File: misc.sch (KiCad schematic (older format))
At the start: 11 parts, among them J11 USB_OTG, U3 LP5900SDX-2.8, U4 AP2204R-3.0TRG1

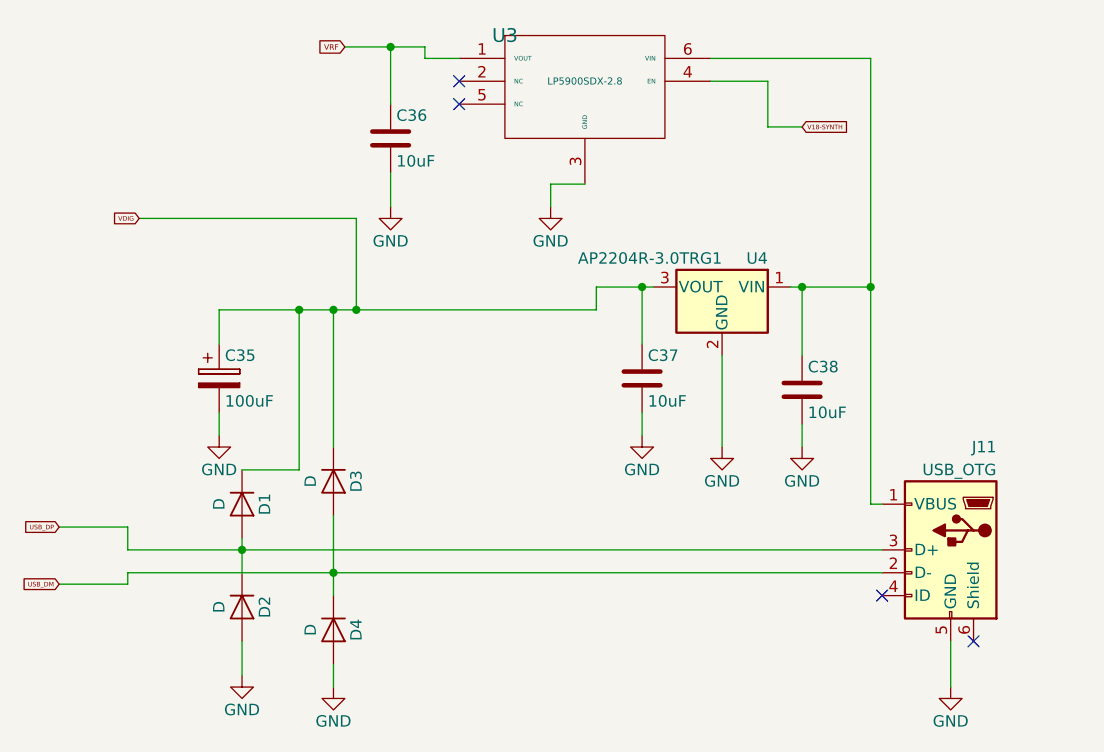
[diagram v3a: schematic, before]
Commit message: use external oscillator repace xtal and add a led
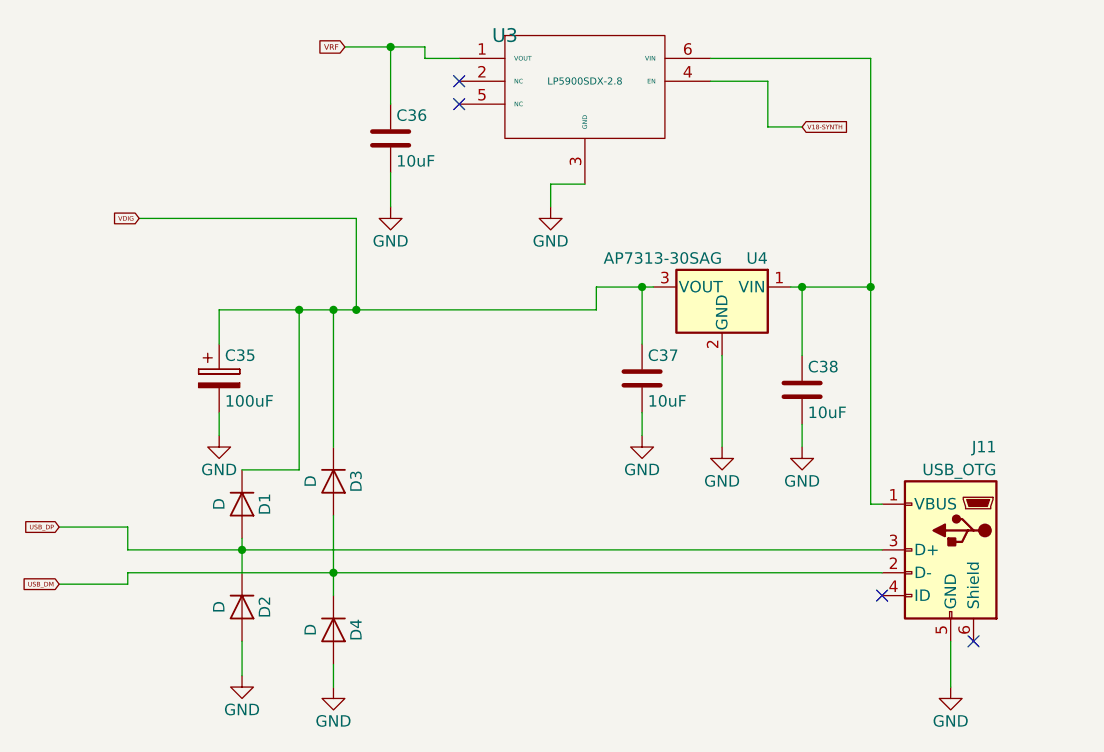
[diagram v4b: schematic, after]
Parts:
- U4: value AP2204R-3.0TRG1 -> AP7313-30SAG
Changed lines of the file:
@@
 Connection ~ 5100 3800
 $Comp
-L GND #PWR36
+L GND #PWR38
 U 1 1 5C690F71
 P 4700 4250
-F 0 "#PWR36" H 4700 4000 50  0001 C CNN
+F 0 "#PWR38" H 4700 4000 50  0001 C CNN
 F 1 "GND" H 4700 4100 50  0000 C CNN
 F 2 "" H 4700 4250 50  0001 C CNN
@@
 $EndComp
 $Comp
-L GND #PWR37
+L GND #PWR39
 U 1 1 5C690F9B
 P 5100 4300
-F 0 "#PWR37" H 5100 4050 50  0001 C CNN
+F 0 "#PWR39" H 5100 4050 50  0001 C CNN
 F 1 "GND" H 5100 4150 50  0000 C CNN
 F 2 "" H 5100 4300 50  0001 C CNN
@@
 	4200 3850 3900 3850
 $Comp
-L GND #PWR35
+L GND #PWR37
 U 1 1 5C6911FA
 P 4600 3200
-F 0 "#PWR35" H 4600 2950 50  0001 C CNN
+F 0 "#PWR37" H 4600 2950 50  0001 C CNN
 F 1 "GND" H 4600 3050 50  0000 C CNN
 F 2 "" H 4600 3200 50  0001 C CNN
@@
 P 6800 2550
 F 0 "U4" H 6600 2675 50  0000 L CNN
-F 1 "AP2204R-3.0TRG1" H 6800 2675 50  0000 L CNN
+F 1 "AP7313-30SAG" H 6800 2675 50  0000 L CNN
 F 2 "TO_SOT_Packages_SMD:SOT-89-3" H 6800 2775 50  0001 C CNN
 F 3 "" H 6800 2550 50  0001 C CNN
@@
 	7150 2550 7150 2850
 $Comp
-L GND #PWR41
+L GND #PWR43
 U 1 1 5C691B40
 P 6800 3250
-F 0 "#PWR41" H 6800 3000 50  0001 C CNN
+F 0 "#PWR43" H 6800 3000 50  0001 C CNN
 F 1 "GND" H 6800 3100 50  0000 C CNN
 F 2 "" H 6800 3250 50  0001 C CNN
@@
 Connection ~ 7150 2550
 $Comp
-L GND #PWR40
+L GND #PWR42
 U 1 1 5C692086
 P 6450 3200
-F 0 "#PWR40" H 6450 2950 50  0001 C CNN
+F 0 "#PWR42" H 6450 2950 50  0001 C CNN
 F 1 "GND" H 6450 3050 50  0000 C CNN
 F 2 "" H 6450 3200 50  0001 C CNN
@@
 $EndComp
 $Comp
-L GND #PWR42
+L GND #PWR44
 U 1 1 5C6920B8
 P 7150 3250
-F 0 "#PWR42" H 7150 3000 50  0001 C CNN
+F 0 "#PWR44" H 7150 3000 50  0001 C CNN
 F 1 "GND" H 7150 3100 50  0000 C CNN
 F 2 "" H 7150 3250 50  0001 C CNN
@@
 	7150 3250 7150 3150
 $Comp
-L GND #PWR39
+L GND #PWR41
 U 1 1 5C69221A
 P 6050 2200
-F 0 "#PWR39" H 6050 1950 50  0001 C CNN
+F 0 "#PWR41" H 6050 1950 50  0001 C CNN
 F 1 "GND" H 6050 2050 50  0000 C CNN
 F 2 "" H 6050 2200 50  0001 C CNN
@@
 Connection ~ 5350 1500
 $Comp
-L GND #PWR38
+L GND #PWR40
 U 1 1 5C692712
 P 5350 2200
-F 0 "#PWR38" H 5350 1950 50  0001 C CNN
+F 0 "#PWR40" H 5350 1950 50  0001 C CNN
 F 1 "GND" H 5350 2050 50  0000 C CNN
 F 2 "" H 5350 2200 50  0001 C CNN
@@
 	6050 2100 6050 2200
 $Comp
-L GND #PWR43
+L GND #PWR45
 U 1 1 5C693D92
 P 7800 4300
-F 0 "#PWR43" H 7800 4050 50  0001 C CNN
+F 0 "#PWR45" H 7800 4050 50  0001 C CNN
 F 1 "GND" H 7800 4150 50  0000 C CNN
 F 2 "" H 7800 4300 50  0001 C CNN

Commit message: replace ldo and finish osc pcb layout
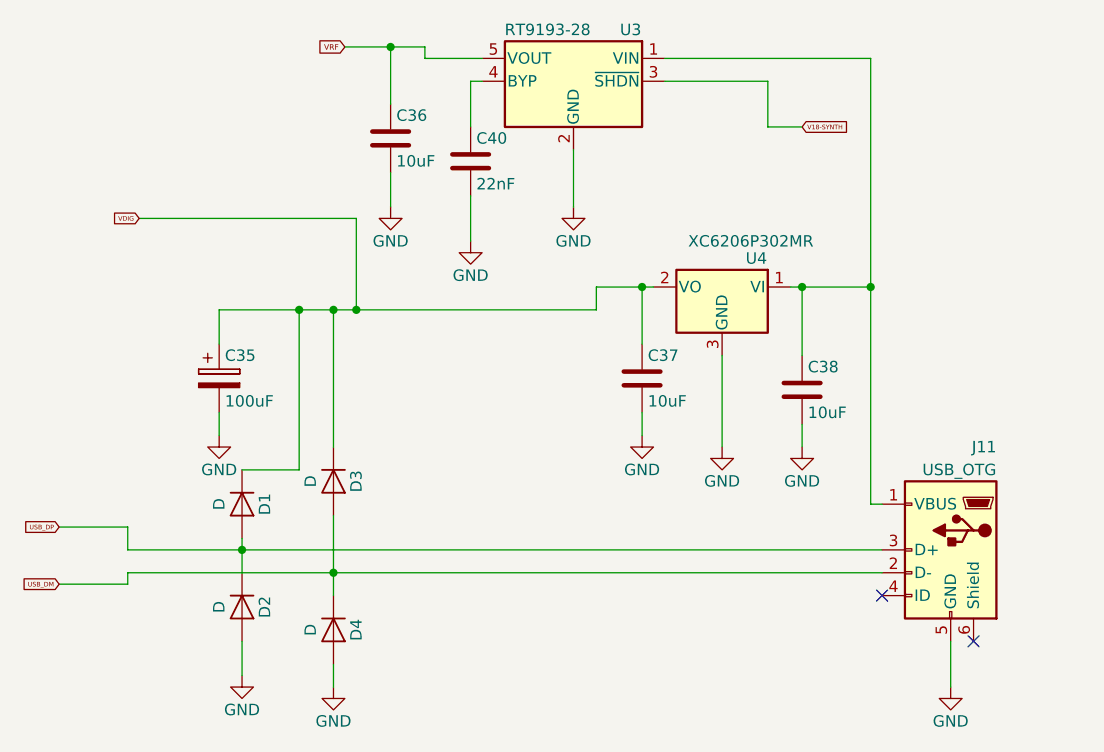
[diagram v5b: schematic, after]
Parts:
- removed U3: LP5900SDX-2.8, Housings_DFN_QFN:DFN-6-1EP_2x2mm_Pitch0.65mm, symbol LP5900SDX-2.8
- removed U4: AP7313-30SAG, TO_SOT_Packages_SMD:SOT-89-3, symbol AP2204R-3.0
- added C40: 22nF, Capacitors_SMD:C_0603, symbol C
- added U3: RT9193-28, TO_SOT_Packages_SMD:SOT-23-5, symbol APE8865Y5-28-HF-3
- added U4: XC6206P302MR, TO_SOT_Packages_SMD:SOT-23, symbol APE8865NR-30-HF-3
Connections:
- net GND: now also C40.2, U3.2 (GND), U4.3 (GND)
- net V18-SYNTH: now also U3.3 (~SHDN~)
- net VDIG: now also U4.2 (VO)
- net VRF: now also U3.5 (VOUT)
- net at C38.1, J11.1 (VBUS): now also U3.1 (VIN), U4.1 (VI)
- new net: C40.1, U3.4 (BYP)
- no-connect marks 4 -> 2
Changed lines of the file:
@@
 Connection ~ 5100 3800
 $Comp
-L GND #PWR38
+L GND #PWR037
 U 1 1 5C690F71
 P 4700 4250
-F 0 "#PWR38" H 4700 4000 50  0001 C CNN
+F 0 "#PWR037" H 4700 4000 50  0001 C CNN
 F 1 "GND" H 4700 4100 50  0000 C CNN
 F 2 "" H 4700 4250 50  0001 C CNN
@@
 $EndComp
 $Comp
-L GND #PWR39
+L GND #PWR038
 U 1 1 5C690F9B
 P 5100 4300
-F 0 "#PWR39" H 5100 4050 50  0001 C CNN
+F 0 "#PWR038" H 5100 4050 50  0001 C CNN
 F 1 "GND" H 5100 4150 50  0000 C CNN
 F 2 "" H 5100 4300 50  0001 C CNN
@@
 	4200 3850 3900 3850
 $Comp
-L GND #PWR37
+L GND #PWR039
 U 1 1 5C6911FA
 P 4600 3200
-F 0 "#PWR37" H 4600 2950 50  0001 C CNN
+F 0 "#PWR039" H 4600 2950 50  0001 C CNN
 F 1 "GND" H 4600 3050 50  0000 C CNN
 F 2 "" H 4600 3200 50  0001 C CNN
@@
 	1    4600 3200
 	1    0    0    -1
-$EndComp
-$Comp
-L AP2204R-3.0 U4
-U 1 1 5C691501
-P 6800 2550
-F 0 "U4" H 6600 2675 50  0000 L CNN
-F 1 "AP7313-30SAG" H 6800 2675 50  0000 L CNN
-F 2 "TO_SOT_Packages_SMD:SOT-89-3" H 6800 2775 50  0001 C CNN
-F 3 "" H 6800 2550 50  0001 C CNN
-	1    6800 2550
-	-1   0    0    -1
 $EndComp
 $Comp
@@
 	7150 2550 7150 2850
 $Comp
-L GND #PWR43
+L GND #PWR040
 U 1 1 5C691B40
 P 6800 3250
-F 0 "#PWR43" H 6800 3000 50  0001 C CNN
+F 0 "#PWR040" H 6800 3000 50  0001 C CNN
 F 1 "GND" H 6800 3100 50  0000 C CNN
 F 2 "" H 6800 3250 50  0001 C CNN
@@
 Connection ~ 7150 2550
 $Comp
-L GND #PWR42
+L GND #PWR041
 U 1 1 5C692086
 P 6450 3200
-F 0 "#PWR42" H 6450 2950 50  0001 C CNN
+F 0 "#PWR041" H 6450 2950 50  0001 C CNN
 F 1 "GND" H 6450 3050 50  0000 C CNN
 F 2 "" H 6450 3200 50  0001 C CNN
@@
 $EndComp
 $Comp
-L GND #PWR44
+L GND #PWR042
 U 1 1 5C6920B8
 P 7150 3250
-F 0 "#PWR44" H 7150 3000 50  0001 C CNN
+F 0 "#PWR042" H 7150 3000 50  0001 C CNN
 F 1 "GND" H 7150 3100 50  0000 C CNN
 F 2 "" H 7150 3250 50  0001 C CNN
@@
 	7150 3250 7150 3150
 $Comp
-L GND #PWR41
+L GND #PWR043
 U 1 1 5C69221A
-P 6050 2200
-F 0 "#PWR41" H 6050 1950 50  0001 C CNN
-F 1 "GND" H 6050 2050 50  0000 C CNN
-F 2 "" H 6050 2200 50  0001 C CNN
-F 3 "" H 6050 2200 50  0001 C CNN
-	1    6050 2200
+P 6150 2200
+F 0 "#PWR043" H 6150 1950 50  0001 C CNN
+F 1 "GND" H 6150 2050 50  0000 C CNN
+F 2 "" H 6150 2200 50  0001 C CNN
+F 3 "" H 6150 2200 50  0001 C CNN
+	1    6150 2200
 	1    0    0    -1
 $EndComp
@@
 VRF
 Wire Wire Line
-	5650 1550 5500 1550
+	5500 1550 5750 1550
 Wire Wire Line
 	5500 1550 5500 1500
@@
 	7000 1850 7000 1650
 Wire Wire Line
-	7000 1650 6750 1650
-NoConn ~ 5650 1650
-NoConn ~ 5650 1750
+	7000 1650 6550 1650
 $Comp
 L C C36
@@
 Connection ~ 5350 1500
 $Comp
-L GND #PWR40
+L GND #PWR044
 U 1 1 5C692712
 P 5350 2200
-F 0 "#PWR40" H 5350 1950 50  0001 C CNN
+F 0 "#PWR044" H 5350 1950 50  0001 C CNN
 F 1 "GND" H 5350 2050 50  0000 C CNN
 F 2 "" H 5350 2200 50  0001 C CNN
@@
 	5350 2200 5350 2050
 Wire Wire Line
-	6750 1550 7450 1550
+	6550 1550 7450 1550
 Connection ~ 7450 2550
 Wire Wire Line
-	6200 2100 6050 2100
-Wire Wire Line
-	6050 2100 6050 2200
-$Comp
-L GND #PWR45
+	6150 1950 6150 2200
+$Comp
+L GND #PWR045
 U 1 1 5C693D92
 P 7800 4300
-F 0 "#PWR45" H 7800 4050 50  0001 C CNN
+F 0 "#PWR045" H 7800 4050 50  0001 C CNN
 F 1 "GND" H 7800 4150 50  0000 C CNN
 F 2 "" H 7800 4300 50  0001 C CNN
@@
 	-1   0    0    -1
 $EndComp
-$Comp
-L LP5900SDX-2.8 U3
-U 1 1 5C6992EB
-P 5850 1450
-F 0 "U3" H 5850 1450 60  0000 C CNN
-F 1 "LP5900SDX-2.8" H 6200 1250 31  0000 C CNN
-F 2 "Housings_DFN_QFN:DFN-6-1EP_2x2mm_Pitch0.65mm" H 5850 1450 60  0001 C CNN
-F 3 "" H 5850 1450 60  0001 C CNN
-	1    5850 1450
-	1    0    0    -1
-$EndComp
 NoConn ~ 7500 3900
 NoConn ~ 7900 4100
@@
 Wire Wire Line
 	4600 3200 4600 3100
+$Comp
+L APE8865NR-30-HF-3 U4
+U 1 1 5CB1DEB2
+P 6800 2550
+F 0 "U4" H 6650 2675 50  0000 C CNN
+F 1 "XC6206P302MR " H 6400 2750 50  0000 L CNN
+F 2 "TO_SOT_Packages_SMD:SOT-23" H 6800 2775 50  0001 C CIN
+F 3 "" H 6800 2500 50  0001 C CNN
+	1    6800 2550
+	-1   0    0    -1
+$EndComp
+$Comp
+L APE8865Y5-28-HF-3 U3
+U 1 1 5CB1E3FD
+P 6150 1650
+F 0 "U3" H 5900 1875 50  0000 C CNN
+F 1 "RT9193-28" H 6075 1875 50  0000 L CNN
+F 2 "TO_SOT_Packages_SMD:SOT-23-5" H 6150 1975 50  0001 C CIN
+F 3 "" H 6150 1750 50  0001 C CNN
+	1    6150 1650
+	-1   0    0    -1
+$EndComp
+$Comp
+L C C40
+U 1 1 5CB1E84A
+P 5700 2000
+F 0 "C40" H 5725 2100 50  0000 L CNN
+F 1 "22nF" H 5725 1900 50  0000 L CNN
+F 2 "Capacitors_SMD:C_0603" H 5738 1850 50  0001 C CNN
+F 3 "" H 5700 2000 50  0001 C CNN
+	1    5700 2000
+	1    0    0    -1
+$EndComp
+$Comp
+L GND #PWR046
+U 1 1 5CB1E8F3
+P 5700 2350
+F 0 "#PWR046" H 5700 2100 50  0001 C CNN
+F 1 "GND" H 5700 2200 50  0000 C CNN
+F 2 "" H 5700 2350 50  0001 C CNN
+F 3 "" H 5700 2350 50  0001 C CNN
+	1    5700 2350
+	1    0    0    -1
+$EndComp
+Wire Wire Line
+	5700 1850 5700 1650
+Wire Wire Line
+	5700 1650 5750 1650
+Wire Wire Line
+	5700 2150 5700 2350
 $EndSCHEMATC
